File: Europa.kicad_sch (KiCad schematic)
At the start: 0 parts

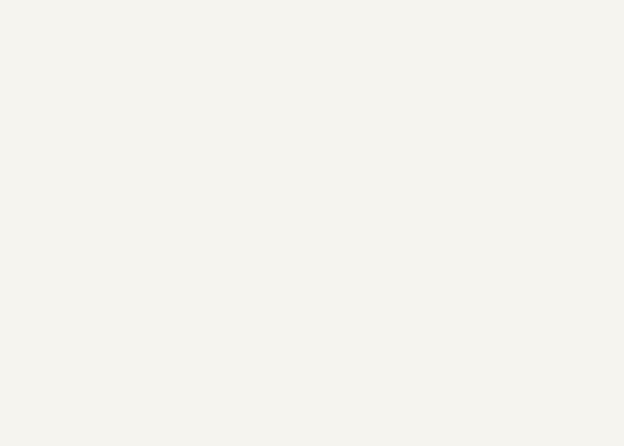
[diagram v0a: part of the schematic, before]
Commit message: Added regulator sheet
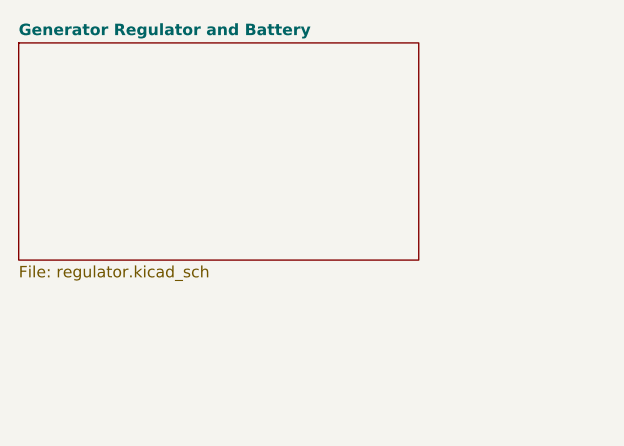
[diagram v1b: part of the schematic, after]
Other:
- added sheet Generator Regulator and Battery (regulator.kicad_sch)
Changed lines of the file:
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@@
+    )
+  )
+  (sheet (at 30.48 29.21) (size 44.45 24.13) (fields_autoplaced)
+    (stroke (width 0.1524) (type solid) (color 0 0 0 0))
+    (fill (color 0 0 0 0.0000))
+    (property "Sheet name" "Generator Regulator and Battery" (id 0) (at 30.48 28.4984 0)
+      (effects (font (size 1.27 1.27) bold) (justify left bottom))
+    )
+    (property "Sheet file" "regulator.kicad_sch" (id 1) (at 30.48 53.9246 0)
+      (effects (font (size 1.27 1.27)) (justify left top))
     )
   )
@@
     (path "/293b5c94-66ed-4931-a87f-688673218b15" (page "2"))
     (path "/75f9b772-c578-422e-a634-635b5097c8a8" (page "3"))
+    (path "/95e96eec-8054-412c-b439-e274da9864da" (page "4"))
   )
   (symbol_instances
@@
       (reference "AE1") (unit 1) (value "Transponder Antenna") (footprint "")
     )
+    (path "/95e96eec-8054-412c-b439-e274da9864da/51d50f68-e9e6-4393-92e3-09fe7c1c92df"
+      (reference "BT?") (unit 1) (value "Battery") (footprint "")
+    )
+    (path "/95e96eec-8054-412c-b439-e274da9864da/2ccf2bcf-c9fa-4aac-8b94-33014b8551f7"
+      (reference "C?") (unit 1) (value "C_Polarized") (footprint "")
+    )
     (path "/293b5c94-66ed-4931-a87f-688673218b15/e89ba836-c472-4e6e-8283-7dec4cf43d20"
       (reference "J1") (unit 1) (value "Antenna SMA") (footprint "")
     )
     (path "/293b5c94-66ed-4931-a87f-688673218b15/ebe3f642-9b43-430a-b037-7f70139ef68a"
-      (reference "J2") (unit 1) (value "DB15_Male") (footprint "")
+      (reference "J2") (unit 1) (value "DB15_Female") (footprint "")
     )
     (path "/293b5c94-66ed-4931-a87f-688673218b15/acbdb600-6467-47ff-9f07-fa11e9815756"
@@
       (reference "J4") (unit 1) (value "Screw_Terminal_01x12") (footprint "")
     )
+    (path "/95e96eec-8054-412c-b439-e274da9864da/58480643-757d-49ce-9d0a-59157dab57c9"
+      (reference "TB3") (unit 1) (value "Terminal_Block_2x12") (footprint "")
+    )
+    (path "/95e96eec-8054-412c-b439-e274da9864da/e9eef6b0-61c9-45dc-a99e-e0a5e09e5289"
+      (reference "U?") (unit 1) (value "Ducati_Regulator") (footprint "")
+    )
   )

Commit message: Added rdac sheet
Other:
- added sheet RDAC (rdac.kicad_sch)
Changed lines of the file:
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@@
+    )
+  )
+  (sheet (at 30.48 74.93) (size 44.45 22.86) (fields_autoplaced)
+    (stroke (width 0.1524) (type solid) (color 0 0 0 0))
+    (fill (color 0 0 0 0.0000))
+    (property "Sheet name" "RDAC" (id 0) (at 30.48 74.2184 0)
+      (effects (font (size 1.27 1.27)) (justify left bottom))
+    )
+    (property "Sheet file" "rdac.kicad_sch" (id 1) (at 30.48 98.3746 0)
+      (effects (font (size 1.27 1.27)) (justify left top))
     )
   )
@@
     (path "/75f9b772-c578-422e-a634-635b5097c8a8" (page "3"))
     (path "/95e96eec-8054-412c-b439-e274da9864da" (page "4"))
+    (path "/a5352cd5-5c6a-411a-b1fe-0b8c42ec40dc" (page "5"))
   )
   (symbol_instances
     (path "/293b5c94-66ed-4931-a87f-688673218b15/f674721b-bb85-4c43-a7cc-c93ff132b271"
       (reference "#PWR01") (unit 1) (value "GND") (footprint "")
+    )
+    (path "/95e96eec-8054-412c-b439-e274da9864da/379a770d-4d17-483a-a138-8c21f91d9801"
+      (reference "#PWR?") (unit 1) (value "GND") (footprint "")
+    )
+    (path "/a5352cd5-5c6a-411a-b1fe-0b8c42ec40dc/4ffc6f8b-ba62-4960-a0b5-48d0f6249e7c"
+      (reference "#PWR?") (unit 1) (value "GND") (footprint "")
+    )
+    (path "/95e96eec-8054-412c-b439-e274da9864da/60f0a32b-297b-4804-b5af-e907dc07f51f"
+      (reference "#PWR?") (unit 1) (value "GND") (footprint "")
+    )
+    (path "/95e96eec-8054-412c-b439-e274da9864da/d8bf2695-17a9-416c-aba7-6777ceba8849"
+      (reference "#PWR?") (unit 1) (value "GND") (footprint "")
     )
     (path "/293b5c94-66ed-4931-a87f-688673218b15/e78f6b9e-11f9-4de0-bf3e-3dfeec8f821c"
@@
     (path "/95e96eec-8054-412c-b439-e274da9864da/2ccf2bcf-c9fa-4aac-8b94-33014b8551f7"
       (reference "C?") (unit 1) (value "C_Polarized") (footprint "")
+    )
+    (path "/a5352cd5-5c6a-411a-b1fe-0b8c42ec40dc/26fb60c6-b782-4115-96e5-0d0a85062e65"
+      (reference "CB?") (unit 1) (value "RDAC CB") (footprint "")
+    )
+    (path "/95e96eec-8054-412c-b439-e274da9864da/17bd44a0-242c-438d-8b3e-1f10aefa7711"
+      (reference "EA1") (unit 1) (value "Engine_Alternator") (footprint "")
+    )
+    (path "/95e96eec-8054-412c-b439-e274da9864da/8d745c97-a2e8-4aae-ae04-665d0442e05a"
+      (reference "F1") (unit 1) (value "Fuse") (footprint "")
+    )
+    (path "/95e96eec-8054-412c-b439-e274da9864da/99fe3586-3050-4444-92a3-76b410a00860"
+      (reference "F2") (unit 1) (value "Fuse") (footprint "")
     )
     (path "/293b5c94-66ed-4931-a87f-688673218b15/e89ba836-c472-4e6e-8283-7dec4cf43d20"
@@
       (reference "J4") (unit 1) (value "Screw_Terminal_01x12") (footprint "")
     )
+    (path "/a5352cd5-5c6a-411a-b1fe-0b8c42ec40dc/76b153a4-0849-40e4-b941-539779425156"
+      (reference "J?") (unit 1) (value "DB25_Female") (footprint "")
+    )
+    (path "/a5352cd5-5c6a-411a-b1fe-0b8c42ec40dc/a0700f3e-8988-4515-a3ad-b2abb0d73540"
+      (reference "J?") (unit 1) (value "DB25_Male") (footprint "")
+    )
+    (path "/a5352cd5-5c6a-411a-b1fe-0b8c42ec40dc/c20d4cbf-03aa-492f-a7cc-6e1124415d77"
+      (reference "J?") (unit 1) (value "DB9_Male") (footprint "")
+    )
+    (path "/a5352cd5-5c6a-411a-b1fe-0b8c42ec40dc/e77952fd-3f26-43bd-9da9-266d1d56298c"
+      (reference "J?") (unit 1) (value "DB9_Female") (footprint "")
+    )
+    (path "/a5352cd5-5c6a-411a-b1fe-0b8c42ec40dc/c010279e-e885-425a-8dde-29e99d1e0e11"
+      (reference "PL10-F") (unit 1) (value "Conn_01x03_Female") (footprint "")
+    )
+    (path "/a5352cd5-5c6a-411a-b1fe-0b8c42ec40dc/94b0ac53-6566-4d3b-8667-5342e6dfb189"
+      (reference "PL10-M") (unit 1) (value "Conn_01x03_Male") (footprint "")
+    )
+    (path "/a5352cd5-5c6a-411a-b1fe-0b8c42ec40dc/2409a3e3-f0dc-4e5d-8d6e-71c8c1c58eb7"
+      (reference "PL12/1") (unit 1) (value "Conn_01x01") (footprint "")
+    )
+    (path "/a5352cd5-5c6a-411a-b1fe-0b8c42ec40dc/32b7ec03-c573-4fc2-9f00-e104d3f42467"
+      (reference "PL15") (unit 1) (value "Conn_01x03_Male") (footprint "")
+    )
+    (path "/95e96eec-8054-412c-b439-e274da9864da/3d5cbab8-4231-4f47-97f4-fa9a7735ee55"
+      (reference "PL15") (unit 1) (value "Conn_01x01") (footprint "")
+    )
+    (path "/95e96eec-8054-412c-b439-e274da9864da/6549f19e-d7ae-423b-90b3-e880a9f61d6c"
+      (reference "PL15") (unit 1) (value "Conn_01x01") (footprint "")
+    )
+    (path "/a5352cd5-5c6a-411a-b1fe-0b8c42ec40dc/73e66a4b-e5f5-4e26-8817-b35fa2e0a76b"
+      (reference "PL15") (unit 1) (value "Conn_01x03_Female") (footprint "")
+    )
+    (path "/95e96eec-8054-412c-b439-e274da9864da/efba767d-032c-4fc0-ac0f-c7b5004e101c"
+      (reference "PL15") (unit 1) (value "Conn_01x01") (footprint "")
+    )
+    (path "/95e96eec-8054-412c-b439-e274da9864da/1c9a909b-961c-49c2-879c-f646c2a2f1a5"
+      (reference "PL15/9") (unit 1) (value "Conn_01x01") (footprint "")
+    )
+    (path "/95e96eec-8054-412c-b439-e274da9864da/d9413806-88d1-4bd0-be4e-3f61d0ad6066"
+      (reference "S?") (unit 1) (value "Starter_Solenoid") (footprint "")
+    )
+    (path "/95e96eec-8054-412c-b439-e274da9864da/f3a2315e-89a5-4ac5-8a4c-516dccff2c50"
+      (reference "S?") (unit 1) (value "Isolator_Solenoid") (footprint "")
+    )
+    (path "/95e96eec-8054-412c-b439-e274da9864da/5a9e00fd-87d6-4f22-8987-36234a7c8cbe"
+      (reference "SM1") (unit 1) (value "Starter_Motor") (footprint "")
+    )
+    (path "/a5352cd5-5c6a-411a-b1fe-0b8c42ec40dc/0270a6e4-ad18-475b-9e92-b0cee3653461"
+      (reference "TB1") (unit 1) (value "Terminal_Block_2x12") (footprint "")
+    )
+    (path "/a5352cd5-5c6a-411a-b1fe-0b8c42ec40dc/8dfbb469-e24c-4918-91c9-d3244a4c0f5f"
+      (reference "TB2") (unit 1) (value "Terminal_Block_2x12") (footprint "")
+    )
     (path "/95e96eec-8054-412c-b439-e274da9864da/58480643-757d-49ce-9d0a-59157dab57c9"

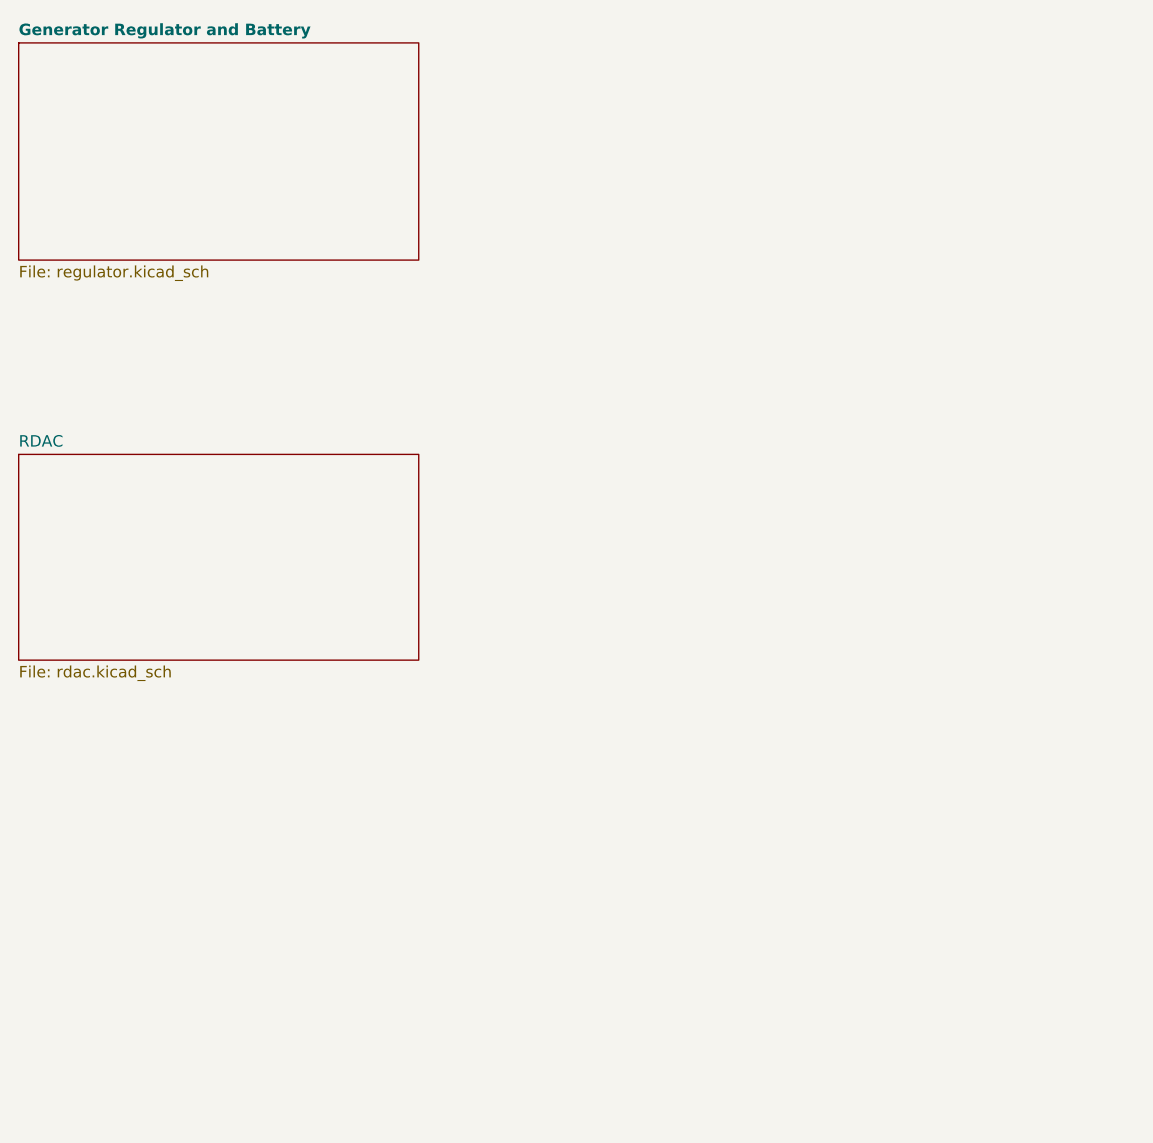
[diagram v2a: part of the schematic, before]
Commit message: Added Main Instrument Panel and Main Bus Panel
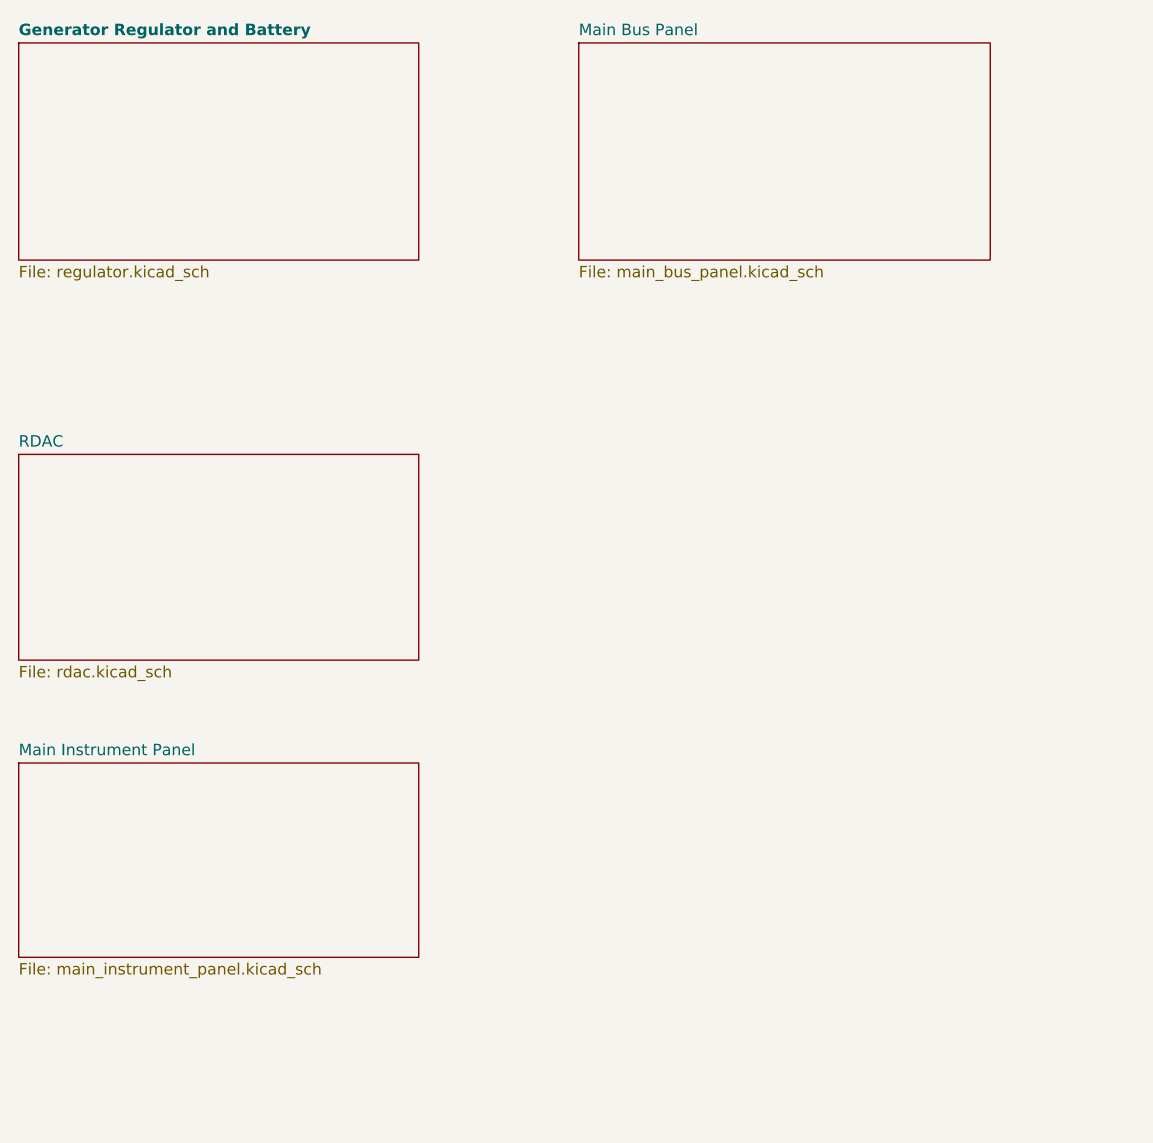
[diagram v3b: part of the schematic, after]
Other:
- added sheet Main Bus Panel (main_bus_panel.kicad_sch)
- added sheet Main Instrument Panel (main_instrument_panel.kicad_sch)
